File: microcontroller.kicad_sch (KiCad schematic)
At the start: 12 parts, among them U4 ESP32-C6-WROOM-1

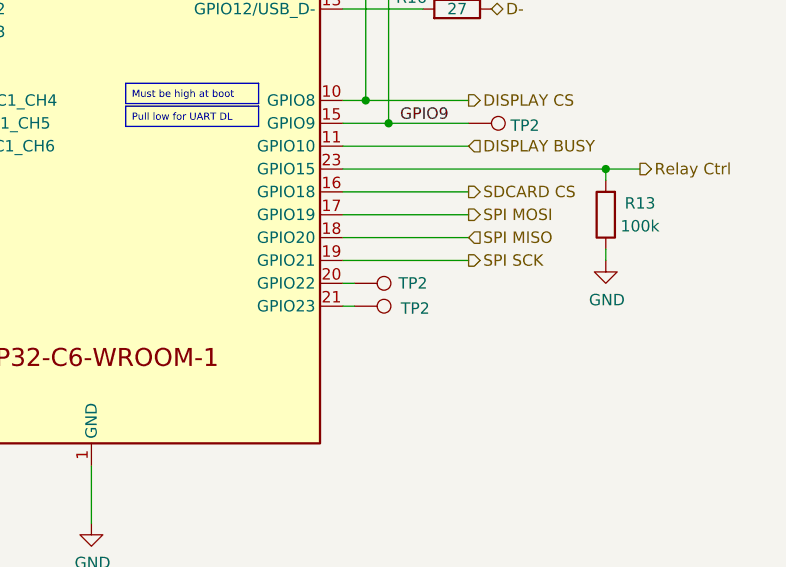
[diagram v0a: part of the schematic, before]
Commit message: V1.2
added reverse mount RGB LED
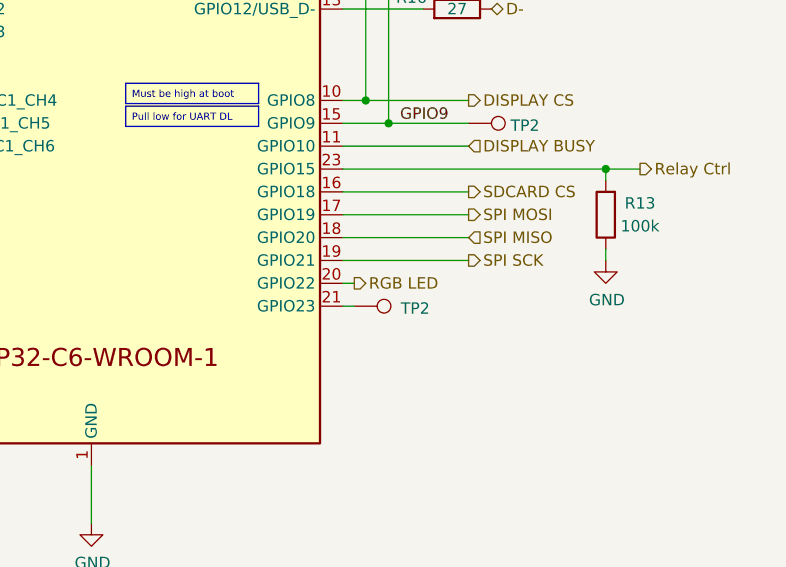
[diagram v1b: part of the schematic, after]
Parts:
- removed TP2: TestPoint, TestPoint:TestPoint_Pad_1.0x1.0mm, symbol Connector:TestPoint
- C9: now in the parts list
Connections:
- net RGB LED: now reaches U4.20 (GPIO22)
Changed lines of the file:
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@@
+    (effects (font (size 1.27 1.27)) (justify left))
+  )
+  (hierarchical_label "RGB LED" (shape output) (at 173.99 104.14 0) (fields_autoplaced)
     (effects (font (size 1.27 1.27)) (justify left))
   )
@@
   )
   (symbol (lib_id "symbols:C") (at 90.17 78.74 0) (mirror y) (unit 1)
-    (exclude_from_sim no) (in_bom no) (on_board yes) (dnp yes)
+    (exclude_from_sim no) (in_bom yes) (on_board yes) (dnp yes)
     (property "Reference" "C9" (at 93.98 80.01 0)
       (effects (font (size 1.27 1.27)) (justify right))
@@
         )
       )
-    )
-  )
-  (symbol (lib_id "Connector:TestPoint") (at 173.99 104.14 270) (unit 1)
-    (exclude_from_sim no) (in_bom yes) (on_board yes) (dnp no)
-    (property "Reference" "TP2" (at 182.118 104.14 90)
-      (effects (font (size 1.27 1.27)) (justify right))
-    )
-    (property "Value" "TestPoint" (at 181.102 112.776 0)
-      (effects (font (size 1.27 1.27)) (justify right) hide)
-    )
-    (property "Footprint" "TestPoint:TestPoint_Pad_1.0x1.0mm" (at 173.99 109.22 0)
-      (effects (font (size 1.27 1.27)) hide)
-    )
-    (property "Datasheet" "~" (at 173.99 109.22 0)
-      (effects (font (size 1.27 1.27)) hide)
-    )
-    (property "Description" "test point" (at 173.99 104.14 0)
-      (effects (font (size 1.27 1.27)) hide)
-    )
-    (pin "1")
-    (instances
-      (project "hh2024"
-        (path "/5f312b85-6822-40a3-b417-2df49696ca2d"
-          (reference "TP2") (unit 1)
-        )
-        (path "/5f312b85-6822-40a3-b417-2df49696ca2d/6c7d4443-00e2-4496-9768-e5d745979ee2"
-          (reference "TP4") (unit 1)
-        )
-      )

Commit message: Small fixes and change footprint library for missing libraries
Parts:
- R32: renamed from R13; value 100k -> 10k; LCSC C2907293 -> C5140188; Link https://www.lcsc.com/product-detail/Chip-span-style-background-color-ff0-Resistor-span-Surface-Mount_FOJAN-FRC0805J104-TS_C2907293.html -> https://www.lcsc.com/product-detail/Chip-span-style-background-color-ff0-Resistor-span-Surface-Mount_VO-SCR0805J10K_C5140188.html
- U1: renamed from U4; footprint tanoshii:ESP32-C6-WROOM-1 -> hh24:ESP32-C6-WROOM-1; Link (none) -> https://www.espressif.com/en/products/socs/esp32-c6
- renumbered C9 to C1, C13 to C4, R16 to R10, R10 to R6, R10 to R7, R10 to R8, R15 to R9, TP2 to TP3, TP2 to TP5
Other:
- company: Nicolai Electronics -> Nicolai Electronics & tilde.industries

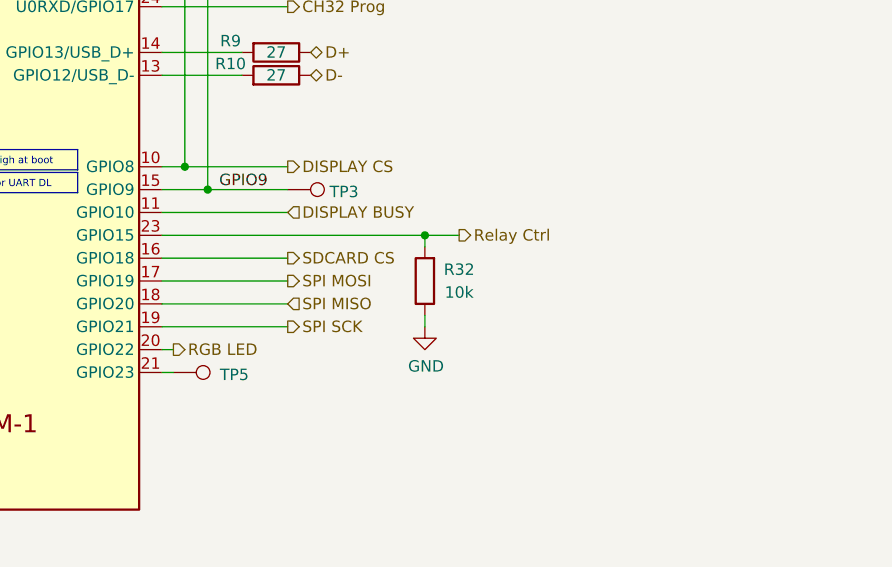
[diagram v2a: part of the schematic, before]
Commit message: Fix power circuit, add headers and move stuff
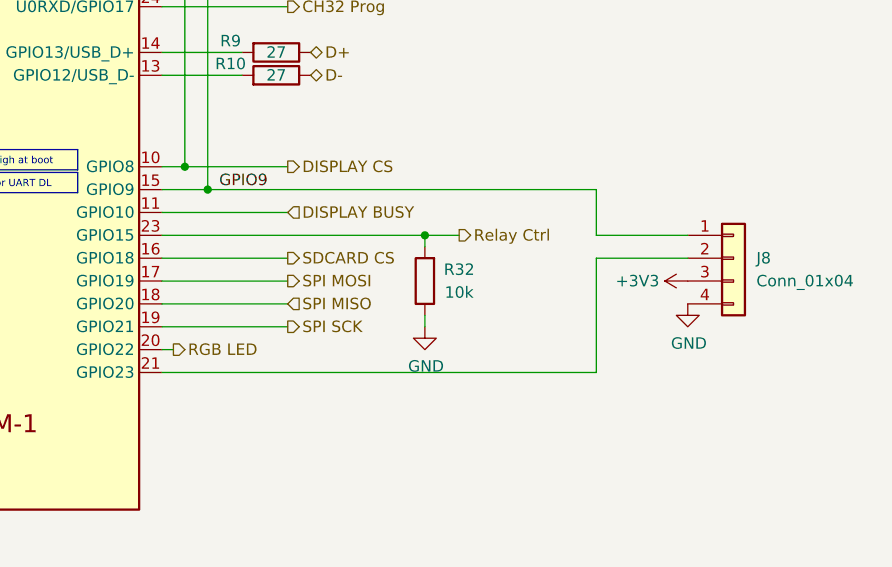
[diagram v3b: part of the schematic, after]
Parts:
- removed TP3, TP5: TestPoint, TestPoint:TestPoint_Pad_1.0x1.0mm, symbol Connector:TestPoint
- added J8: Conn_01x04, Connector_PinHeader_2.54mm:PinHeader_1x04_P2.54mm_Vertical, symbol Connector_Generic:Conn_01x04
- R6, R7, R8: LCSC C5140188 -> C5140188
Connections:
- net +3V3: now also J8.3 (Pin_3)
- net GND: now also J8.4 (Pin_4)
- net GPIO9: now also J8.1 (Pin_1)
- net at U1.21 (GPIO23): now also J8.2 (Pin_2)

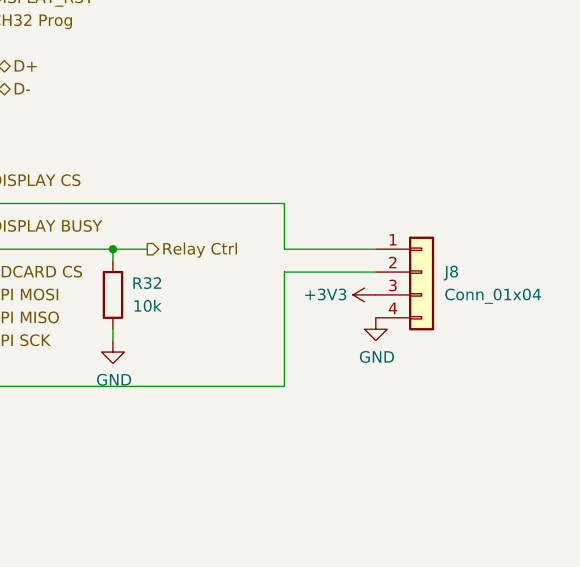
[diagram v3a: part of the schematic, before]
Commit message: Added artwork (cont)
DRC pass
Removed header from the BoM
changed the relay header to SMD so it doesn't clash with art
made header for CH32 prog THT
Moved designators in reasonable place
added hacker hotel and badge.team artwork
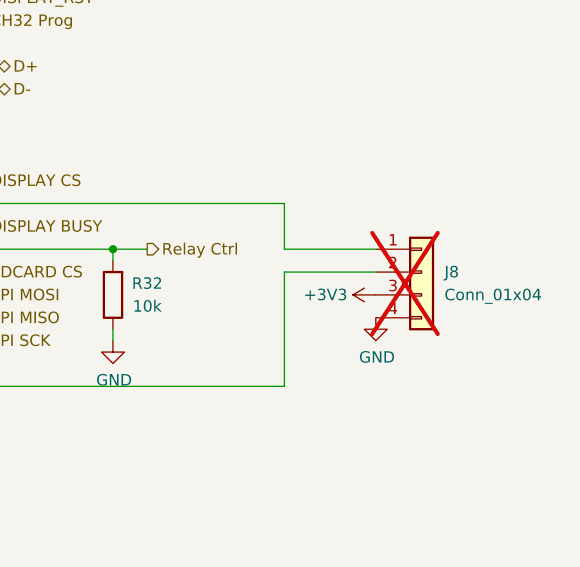
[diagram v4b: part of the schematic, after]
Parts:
- J8: now not fitted; now left out of the parts list
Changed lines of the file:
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@@
 		(unit 1)
 		(exclude_from_sim no)
-		(in_bom yes)
+		(in_bom no)
 		(on_board yes)
-		(dnp no)
+		(dnp yes)
 		(fields_autoplaced yes)
 		(property "Reference" "J8"
@@
 			(at 236.22 93.98 0)
 			(effects
+				(font
+					(size 1.27 1.27)
+				)
+				(hide yes)
+			)
+		)
+		(property "Link" ""
+			(at 236.22 93.98 0)
+			(effects

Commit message: Moar headers
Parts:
- renumbered C4 to C2, C1 to C3, R6 to R17, R7 to R18, R8 to R19, R9 to R20, R10 to R21, R32 to R22, U1 to U3
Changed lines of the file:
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@@
 		(on_board yes)
 		(dnp no)
-		(property "Reference" "#PWR023"
+		(property "Reference" "#PWR045"
 			(at 231.14 105.41 0)
 			(effects
@@
 			(project "hh2024"
 				(path "/5f312b85-6822-40a3-b417-2df49696ca2d/6c7d4443-00e2-4496-9768-e5d745979ee2"
-					(reference "#PWR023")
+					(reference "#PWR045")
 					(unit 1)
 				)
@@
 		(on_board yes)
 		(dnp no)
-		(property "Reference" "R8"
+		(property "Reference" "R19"
 			(at 181.61 58.42 0)
 			(effects
@@
 			(project "hh2024"
 				(path "/5f312b85-6822-40a3-b417-2df49696ca2d/6c7d4443-00e2-4496-9768-e5d745979ee2"
-					(reference "R8")
+					(reference "R19")
 					(unit 1)
 				)
@@
 		(on_board yes)
 		(dnp no)
-		(property "Reference" "R6"
+		(property "Reference" "R17"
 			(at 93.98 57.15 0)
 			(effects
@@
 			(project "hh2024"
 				(path "/5f312b85-6822-40a3-b417-2df49696ca2d/6c7d4443-00e2-4496-9768-e5d745979ee2"
-					(reference "R6")
+					(reference "R17")
 					(unit 1)
 				)
@@
 		(on_board yes)
 		(dnp no)
-		(property "Reference" "C4"
+		(property "Reference" "C2"
 			(at 79.121 57.2516 0)
 			(effects
@@
 			(project "hh2024"
 				(path "/5f312b85-6822-40a3-b417-2df49696ca2d/6c7d4443-00e2-4496-9768-e5d745979ee2"
-					(reference "C4")
+					(reference "C2")
 					(unit 1)
 				)
@@
 		(on_board yes)
 		(dnp no)
-		(property "Reference" "#PWR021"
+		(property "Reference" "#PWR038"
 			(at 90.17 58.42 0)
 			(effects
@@
 			(project "hh2024"
 				(path "/5f312b85-6822-40a3-b417-2df49696ca2d/6c7d4443-00e2-4496-9768-e5d745979ee2"
-					(reference "#PWR021")
+					(reference "#PWR038")
 					(unit 1)
 				)
@@
 		(on_board yes)
 		(dnp no)
-		(property "Reference" "#PWR05"
+		(property "Reference" "#PWR043"
 			(at 201.93 107.95 0)
 			(effects
@@
 			(project "hh2024"
 				(path "/5f312b85-6822-40a3-b417-2df49696ca2d/6c7d4443-00e2-4496-9768-e5d745979ee2"
-					(reference "#PWR05")
+					(reference "#PWR043")
 					(unit 1)
 				)
@@
 		(on_board yes)
 		(dnp no)
-		(property "Reference" "#PWR024"
+		(property "Reference" "#PWR044"
 			(at 234.95 96.52 0)
 			(effects
@@
 			(project "hh2024"
 				(path "/5f312b85-6822-40a3-b417-2df49696ca2d/6c7d4443-00e2-4496-9768-e5d745979ee2"
-					(reference "#PWR024")
+					(reference "#PWR044")
 					(unit 1)
 				)
@@
 		(on_board yes)
 		(dnp no)
-		(property "Reference" "#PWR028"
+		(property "Reference" "#PWR041"
 			(at 144.78 137.16 0)
 			(effects
@@
 			(project "hh2024"
 				(path "/5f312b85-6822-40a3-b417-2df49696ca2d/6c7d4443-00e2-4496-9768-e5d745979ee2"
-					(reference "#PWR028")
+					(reference "#PWR041")
 					(unit 1)
 				)
@@
 		(on_board yes)
 		(dnp no)
-		(property "Reference" "R32"
+		(property "Reference" "R22"
 			(at 205.74 95.25 0)
 			(effects
@@
 			(project "hh2024"
 				(path "/5f312b85-6822-40a3-b417-2df49696ca2d/6c7d4443-00e2-4496-9768-e5d745979ee2"
-					(reference "R32")
+					(reference "R22")
 					(unit 1)
 				)
@@
 		(on_board yes)
 		(dnp no)
-		(property "Reference" "#PWR029"
+		(property "Reference" "#PWR042"
 			(at 176.53 55.88 0)
 			(effects
@@
 			(project "hh2024"
 				(path "/5f312b85-6822-40a3-b417-2df49696ca2d/6c7d4443-00e2-4496-9768-e5d745979ee2"
-					(reference "#PWR029")
+					(reference "#PWR042")
 					(unit 1)
 				)
@@
 		(on_board yes)
 		(dnp yes)
-		(property "Reference" "C1"
+		(property "Reference" "C3"
 			(at 93.98 80.01 0)
 			(effects
@@
 			(project "hh2024"
 				(path "/5f312b85-6822-40a3-b417-2df49696ca2d/6c7d4443-00e2-4496-9768-e5d745979ee2"
-					(reference "C1")
+					(reference "C3")
 					(unit 1)
 				)
@@
 		(on_board yes)
 		(dnp no)
-		(property "Reference" "#PWR027"
+		(property "Reference" "#PWR040"
 			(at 144.78 57.15 0)
 			(effects
@@
 			(project "hh2024"
 				(path "/5f312b85-6822-40a3-b417-2df49696ca2d/6c7d4443-00e2-4496-9768-e5d745979ee2"
-					(reference "#PWR027")
+					(reference "#PWR040")
 					(unit 1)
 				)
@@
 		(on_board yes)
 		(dnp no)
-		(property "Reference" "R7"
+		(property "Reference" "R18"
 			(at 171.45 55.88 0)
 			(effects
@@
 			(project "hh2024"
 				(path "/5f312b85-6822-40a3-b417-2df49696ca2d/6c7d4443-00e2-4496-9768-e5d745979ee2"
-					(reference "R7")
+					(reference "R18")
 					(unit 1)
 				)
@@
 		(on_board yes)
 		(dnp no)
-		(property "Reference" "#PWR022"
+		(property "Reference" "#PWR039"
 			(at 90.17 88.9 0)
 			(effects
@@
 			(project "hh2024"
 				(path "/5f312b85-6822-40a3-b417-2df49696ca2d/6c7d4443-00e2-4496-9768-e5d745979ee2"
-					(reference "#PWR022")
+					(reference "#PWR039")
 					(unit 1)
 				)
@@
 		(on_board yes)
 		(dnp no)
-		(property "Reference" "#PWR026"
+		(property "Reference" "#PWR037"
 			(at 76.2 68.58 0)
 			(effects
@@
 			(project "hh2024"
 				(path "/5f312b85-6822-40a3-b417-2df49696ca2d/6c7d4443-00e2-4496-9768-e5d745979ee2"
-					(reference "#PWR026")
+					(reference "#PWR037")
 					(unit 1)
 				)
@@
 		(on_board yes)
 		(dnp no)
-		(property "Reference" "#PWR025"
+		(property "Reference" "#PWR036"
 			(at 76.2 58.42 0)
 			(effects
@@
 			(project "hh2024"
 				(path "/5f312b85-6822-40a3-b417-2df49696ca2d/6c7d4443-00e2-4496-9768-e5d745979ee2"
-					(reference "#PWR025")
+					(reference "#PWR036")
 					(unit 1)
 				)
@@
 		(on_board yes)
 		(dnp no)
-		(property "Reference" "R10"
+		(property "Reference" "R21"
 			(at 180.34 72.39 90)
 			(effects
@@
 			(project "hh2024"
 				(path "/5f312b85-6822-40a3-b417-2df49696ca2d/6c7d4443-00e2-4496-9768-e5d745979ee2"
-					(reference "R10")
+					(reference "R21")
 					(unit 1)
 				)
@@
 		(on_board yes)
 		(dnp no)
-		(property "Reference" "R9"
+		(property "Reference" "R20"
 			(at 180.34 69.85 90)
 			(effects
@@
 			(project "hh2024"
 				(path "/5f312b85-6822-40a3-b417-2df49696ca2d/6c7d4443-00e2-4496-9768-e5d745979ee2"
-					(reference "R9")
+					(reference "R20")
 					(unit 1)
 				)
@@
 		(dnp no)
 		(fields_autoplaced yes)
-		(property "Reference" "U1"
+		(property "Reference" "U3"
 			(at 146.7359 55.88 0)
 			(effects
@@
 			(project "hh2024"
 				(path "/5f312b85-6822-40a3-b417-2df49696ca2d/6c7d4443-00e2-4496-9768-e5d745979ee2"
-					(reference "U1")
-					(unit 1)
-				)
+					(reference "U3")
+					(unit 1)
+				)
